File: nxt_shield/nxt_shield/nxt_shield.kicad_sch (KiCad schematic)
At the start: 87 parts, among them J1 NXT_M0, J10 NXT_SENS0, J11 NXT_SENS0, J12 NXT_SENS0, J13 NXT_SENS0, J14 NXT_SENS0, J15 NXT_SENS0, J16 NXT_SENS0, J17 RB_I2C1, J18 RB_I2C0, J19 RB_I2C2, J2 RB_M0, J20 RB_I2C3, J21 RB_I2C4, J22 RB_I2C5, J23 RB_I2C6, J24 RB_I2C7, J25 RB_Power, J3 NXT_SENS0, J4 RB_M0, J5 NXT_M1, J6 RB_M0, J7 NXT_M2, J8 LCD, U1 74HC14, U3 TPS4H000, U6 TPS4H000

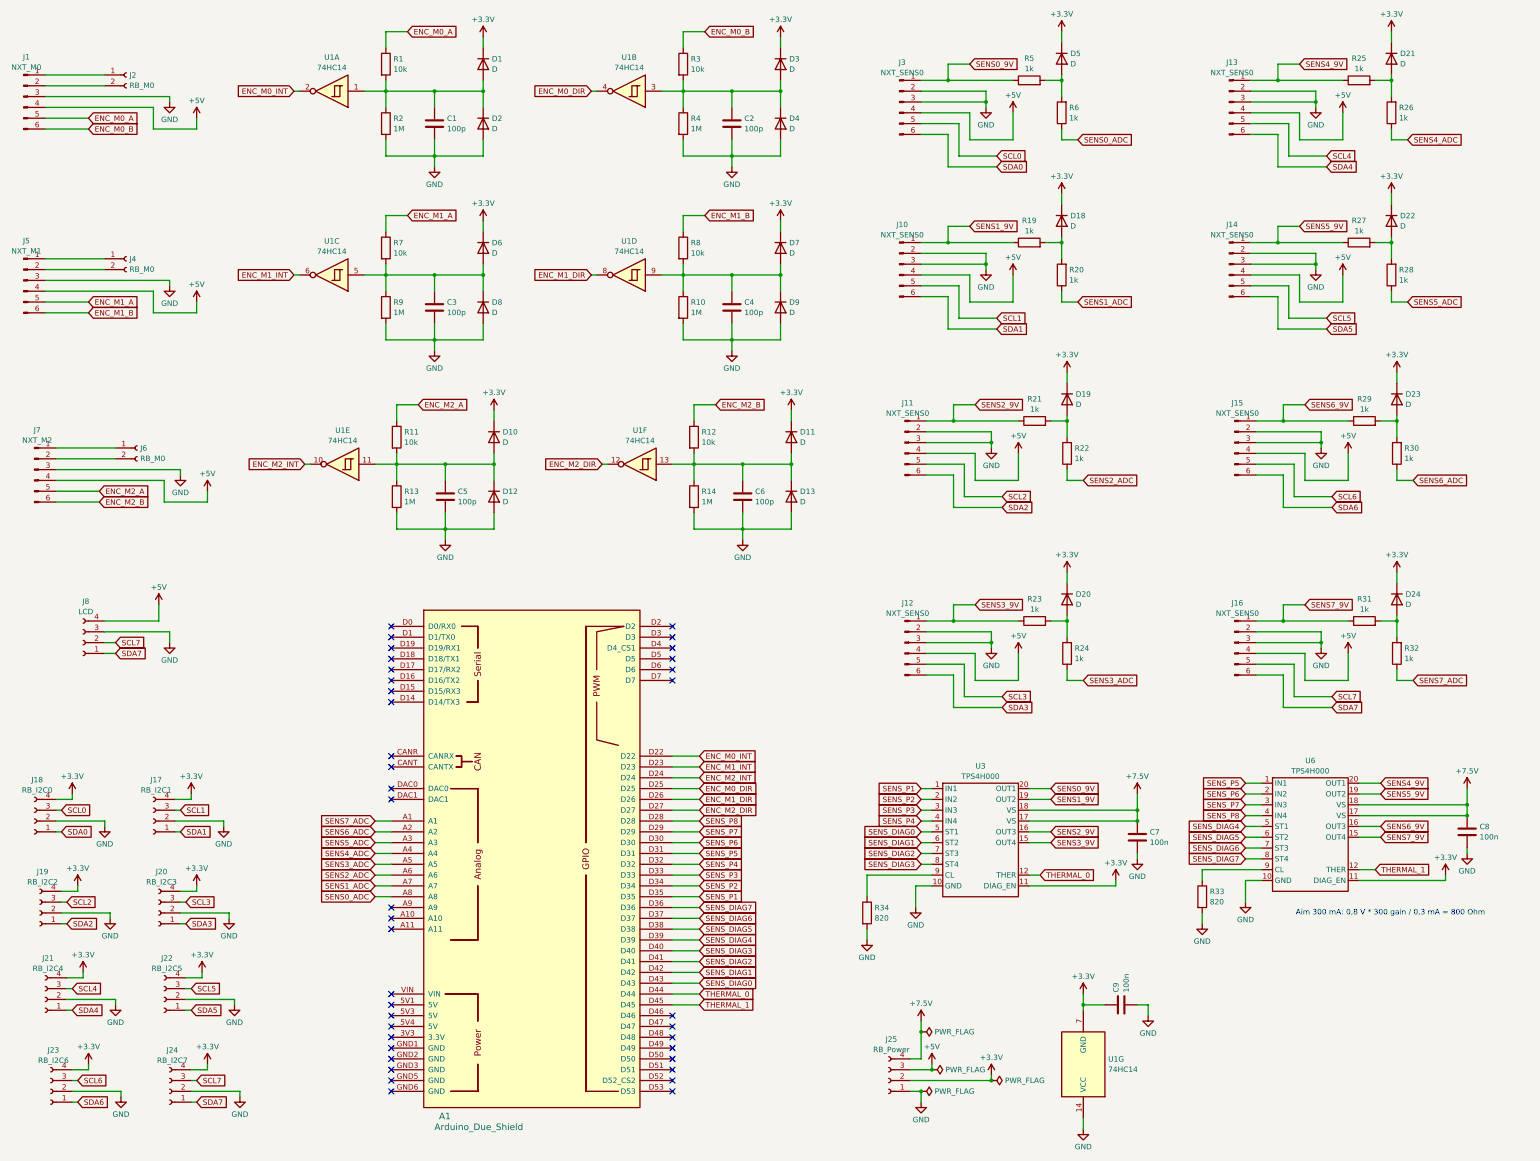
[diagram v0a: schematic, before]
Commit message: first version of NXT shield with nxt sensors
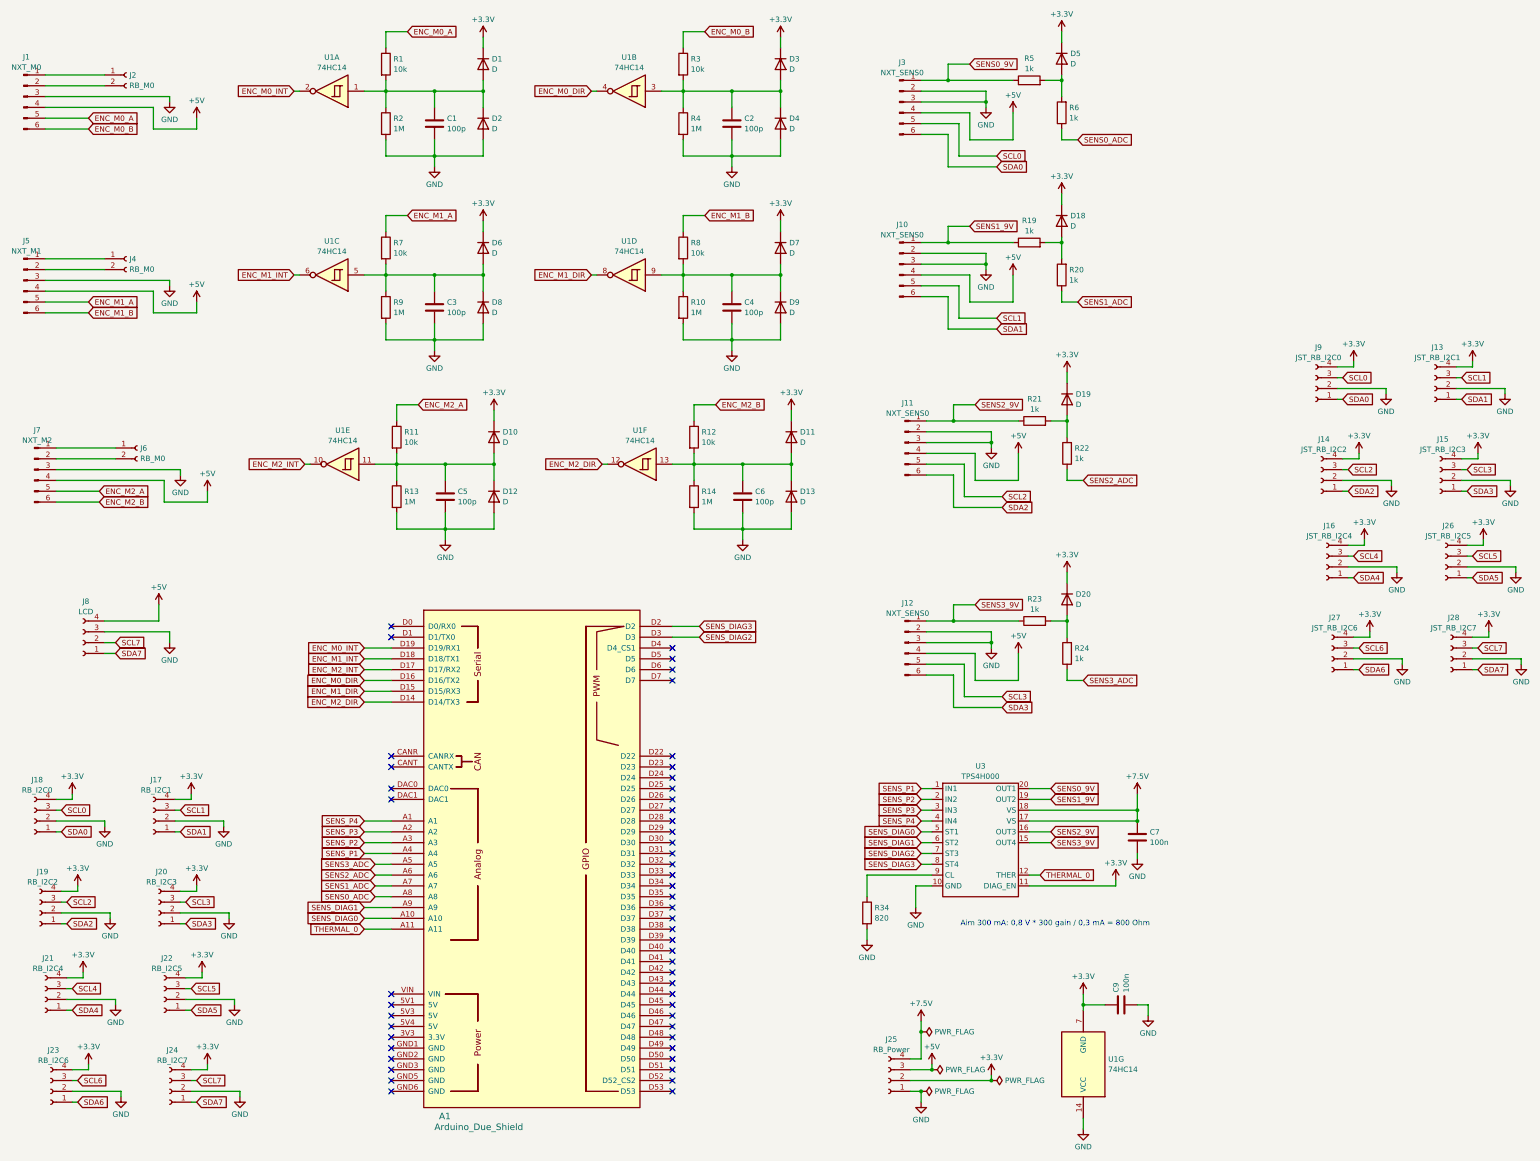
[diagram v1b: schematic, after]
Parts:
- removed C8: 100n, Capacitor_SMD:C_0603_1608Metric, symbol Device:C
- removed D21, D22, D23, D24: D, Diode_SMD:D_0603_1608Metric, symbol Device:D
- removed J13, J14, J15, J16: NXT_SENS0, Connector_RJ:RJ25_Wayconn_MJEA-660X1_Horizontal, symbol Connector:Conn_01x06_Pin
- removed R25, R26, R27, R28, R29, R30, R31, R32: 1k, Resistor_SMD:R_0603_1608Metric, symbol Device:R
- removed R33: 820, Resistor_SMD:R_0603_1608Metric, symbol Device:R
- removed U6: TPS4H000, Package_SO:HTSSOP-20-1EP_4.4x6.5mm_P0.65mm_EP2.74x3.86mm, symbol TPS4H000:TPS4H000
- added J13: JST_RB_I2C1, Connector_JST:JST_PH_B4B-PH-K_1x04_P2.00mm_Vertical, symbol Connector:Conn_01x04_Socket
- added J14: JST_RB_I2C2, Connector_JST:JST_PH_B4B-PH-K_1x04_P2.00mm_Vertical, symbol Connector:Conn_01x04_Socket
- added J15: JST_RB_I2C3, Connector_JST:JST_PH_B4B-PH-K_1x04_P2.00mm_Vertical, symbol Connector:Conn_01x04_Socket
- added J16: JST_RB_I2C4, Connector_JST:JST_PH_B4B-PH-K_1x04_P2.00mm_Vertical, symbol Connector:Conn_01x04_Socket
- added J26: JST_RB_I2C5, Connector_JST:JST_PH_B4B-PH-K_1x04_P2.00mm_Vertical, symbol Connector:Conn_01x04_Socket
- added J27: JST_RB_I2C6, Connector_JST:JST_PH_B4B-PH-K_1x04_P2.00mm_Vertical, symbol Connector:Conn_01x04_Socket
- added J28: JST_RB_I2C7, Connector_JST:JST_PH_B4B-PH-K_1x04_P2.00mm_Vertical, symbol Connector:Conn_01x04_Socket
- added J9: JST_RB_I2C0, Connector_JST:JST_PH_B4B-PH-K_1x04_P2.00mm_Vertical, symbol Connector:Conn_01x04_Socket
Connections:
- net SENS4_ADC is gone; now on net SENS_P1: A1.A4
- net SENS5_ADC is gone; now on net SENS_P2: A1.A3
- net SENS6_ADC is gone; now on net SENS_P3: A1.A2
- net SENS7_ADC is gone; now on net SENS_P4: A1.A1
- net +3.3V: now also J13.4 (Pin_4), J14.4 (Pin_4), J15.4 (Pin_4), J16.4 (Pin_4), J26.4 (Pin_4), J27.4 (Pin_4), J28.4 (Pin_4), J9.4 (Pin_4)
- net ENC_M0_DIR: now also A1.D16 (D16/TX2); no longer A1.D25
- net ENC_M0_INT: now also A1.D19 (D19/RX1); no longer A1.D22
- net ENC_M1_DIR: now also A1.D15 (D15/RX3); no longer A1.D26
- net ENC_M1_INT: now also A1.D18 (D18/TX1); no longer A1.D23
- net ENC_M2_DIR: now also A1.D14 (D14/TX3); no longer A1.D27
- net ENC_M2_INT: now also A1.D17 (D17/RX2); no longer A1.D24
- net GND: now also J13.2 (Pin_2), J14.2 (Pin_2), J15.2 (Pin_2), J16.2 (Pin_2), J26.2 (Pin_2), J27.2 (Pin_2), J28.2 (Pin_2), J9.2 (Pin_2)
- net SCL0: now also J9.3 (Pin_3)
- net SCL1: now also J13.3 (Pin_3)
- net SCL2: now also J14.3 (Pin_3)
- net SCL3: now also J15.3 (Pin_3)
- net SCL4: now also J16.3 (Pin_3)
- net SCL5: now also J26.3 (Pin_3)
- net SCL6: now also J27.3 (Pin_3)
- net SCL7: now also J28.3 (Pin_3)
- net SDA0: now also J9.1 (Pin_1)
- net SDA1: now also J13.1 (Pin_1)
- net SDA2: now also J14.1 (Pin_1)
- net SDA3: now also J15.1 (Pin_1)
- net SDA4: now also J16.1 (Pin_1)
- net SDA5: now also J26.1 (Pin_1)
- net SDA6: now also J27.1 (Pin_1)
- net SDA7: now also J28.1 (Pin_1)
- net SENS_DIAG0: now also A1.A10; no longer A1.D43
- net SENS_DIAG1: now also A1.A9; no longer A1.D42
- net SENS_DIAG2: now also A1.D3; no longer A1.D41
- net SENS_DIAG3: now also A1.D2; no longer A1.D40
- net SENS_P1: no longer A1.D35
- net SENS_P2: no longer A1.D34
- net SENS_P3: no longer A1.D33
- net SENS_P4: no longer A1.D32
- net THERMAL_0: now also A1.A11; no longer A1.D44
- net SENS_DIAG4: no longer names the net of A1.D39
- net SENS_DIAG5: no longer names the net of A1.D38
- net SENS_DIAG6: no longer names the net of A1.D37
- net SENS_DIAG7: no longer names the net of A1.D36
- net SENS_P5: no longer names the net of A1.D31
- net SENS_P6: no longer names the net of A1.D30
- net SENS_P7: no longer names the net of A1.D29
- net SENS_P8: no longer names the net of A1.D28
- net THERMAL_1: no longer names the net of A1.D45
- no-connect marks 39 -> 52

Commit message: nxt shield first prototype production
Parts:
- removed C7: 100n, Capacitor_SMD:C_0603_1608Metric, symbol Device:C
- removed D18, D19, D20, D5: D, Diode_SMD:D_0603_1608Metric, symbol Device:D
- removed J10, J11, J12, J3: NXT_SENS0, Connector_RJ:RJ25_Wayconn_MJEA-660X1_Horizontal, symbol Connector:Conn_01x06_Pin
- removed R19, R20, R21, R22, R23, R24, R5, R6: 1k, Resistor_SMD:R_0603_1608Metric, symbol Device:R
- removed R34: 820, Resistor_SMD:R_0603_1608Metric, symbol Device:R
- removed U3: TPS4H000, Package_SO:HTSSOP-20-1EP_4.4x6.5mm_P0.65mm_EP2.74x3.86mm, symbol TPS4H000:TPS4H000
- added J10: XT60_Case, Connector_AMASS:AMASS_XT60IPW-M_1x03_P7.20mm_Horizontal, symbol Connector:Conn_01x02_Pin
- added J3: XT60_PCB, Connector_AMASS:AMASS_XT60-M_1x02_P7.20mm_Vertical, symbol Connector:Conn_01x02_Pin
- added SW1, SW2, SW3: SW_Push, Button_Switch_THT:SW_PUSH_6mm, symbol Switch:SW_Push
- added SW4: SW_SPDT, CustomFootprints:XKB Connection SS-12M11G5, symbol Switch:SW_SPDT
- C1, C2, C3, C4, C5, C6, C9: footprint Capacitor_SMD:C_0603_1608Metric -> Capacitor_SMD:C_0805_2012Metric_Pad1.18x1.45mm_HandSolder
- D1, D10, D11, D12, D13, D2, D3, D4, D6, D7, D8, D9: footprint Diode_SMD:D_0603_1608Metric -> Diode_SMD:D_0805_2012Metric_Pad1.15x1.40mm_HandSolder
- J8: footprint Connector_PinSocket_2.54mm:PinSocket_1x04_P2.54mm_Vertical -> CustomFootprints:OLE_LCD
- R1, R10, R11, R12, R13, R14, R2, R3, R4, R7, R8, R9: footprint Resistor_SMD:R_0603_1608Metric -> Resistor_SMD:R_0805_2012Metric_Pad1.20x1.40mm_HandSolder
- U1: footprint Package_SO:SOIC-14-16_3.9x9.9mm_P1.27mm -> Package_SO:SO-14_3.9x8.65mm_P1.27mm
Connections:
- net +3.3V: no longer J13.4 (Pin_4), J14.4 (Pin_4), J15.4 (Pin_4), J16.4 (Pin_4), J17.4 (Pin_4), J18.4 (Pin_4), J19.4 (Pin_4), J20.4 (Pin_4), J21.4 (Pin_4), J22.4 (Pin_4), J23.4 (Pin_4), J24.4 (Pin_4), J26.4 (Pin_4), J27.4 (Pin_4), J28.4 (Pin_4), J9.4 (Pin_4)
- net +5V: now also J8.3 (Pin_3); no longer J8.4 (Pin_4)
- net GND: now also J8.4 (Pin_4), J10.1 (Pin_1), J3.1 (Pin_1), SW1.2, SW2.2, SW3.2; no longer J8.3 (Pin_3)
- net M1A: now reaches J4.1 (Pin_1), J5.1 (Pin_1)
- net M1B: now reaches J4.2 (Pin_2), J5.2 (Pin_2)
- net M2A: now reaches J6.1 (Pin_1), J7.1 (Pin_1)
- net M2B: now reaches J6.2 (Pin_2), J7.2 (Pin_2)
- net M0A: now reaches J1.1 (Pin_1), J2.1 (Pin_1)
- net M0B: now reaches J1.2 (Pin_2), J2.2 (Pin_2)
- net SENS0_ADC: no longer names the net of A1.A8
- net SENS1_ADC: no longer names the net of A1.A7
- net SENS2_ADC: no longer names the net of A1.A6
- net SENS3_ADC: no longer names the net of A1.A5
- net SENS_DIAG0 renamed Button2
- net Button2: now also SW2.1
- net SENS_DIAG1 renamed Button1
- net Button1: now also SW1.1
- net SENS_DIAG2: no longer names the net of A1.D3
- net SENS_DIAG3: no longer names the net of A1.D2
- net SENS_P1: no longer names the net of A1.A4
- net SENS_P2: no longer names the net of A1.A3
- net SENS_P3: no longer names the net of A1.A2
- net SENS_P4: no longer names the net of A1.A1
- net THERMAL_0 renamed Button3
- net Button3: now also SW3.1
- new net AKKU1: J3.2 (Pin_2), SW4.2 (B)
- new net AKKU2: J10.2 (Pin_2), SW4.3 (C)
- new net VDDI2C0: J18.4 (Pin_4), J9.4 (Pin_4)
- new net VDDI2C1: J13.4 (Pin_4), J17.4 (Pin_4)
- new net VDDI2C2: J14.4 (Pin_4), J19.4 (Pin_4)
- new net VDDI2C3: J15.4 (Pin_4), J20.4 (Pin_4)
- new net VDDI2C4: J16.4 (Pin_4), J21.4 (Pin_4)
- new net VDDI2C5: J22.4 (Pin_4), J26.4 (Pin_4)
- new net VDDI2C6: J23.4 (Pin_4), J27.4 (Pin_4)
- new net VDDI2C7: J24.4 (Pin_4), J28.4 (Pin_4)
- no-connect marks 52 -> 62
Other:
- note removed: "Aim 300 mA: 0,8 V * 300 gain / 0,3 mA = 800 Ohm"
- moved on the sheet: C9, J13, J14, J15, J16, J25, J26, J27, J28, J9, U1G
